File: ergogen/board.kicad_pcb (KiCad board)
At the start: 2 copper layers, 154.2 x 107.9 mm, 58 parts

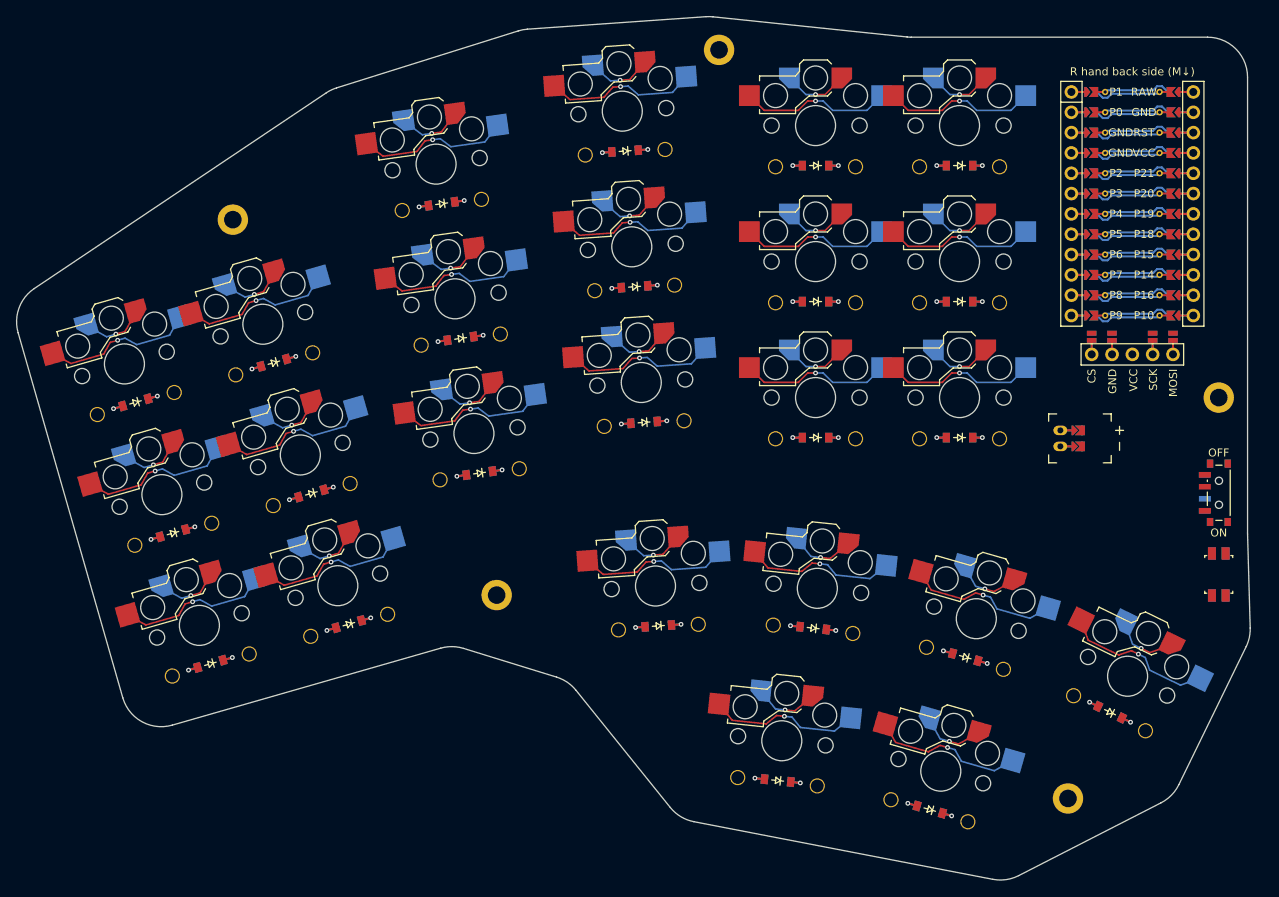
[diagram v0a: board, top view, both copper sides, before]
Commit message: making layout changes for easier routing
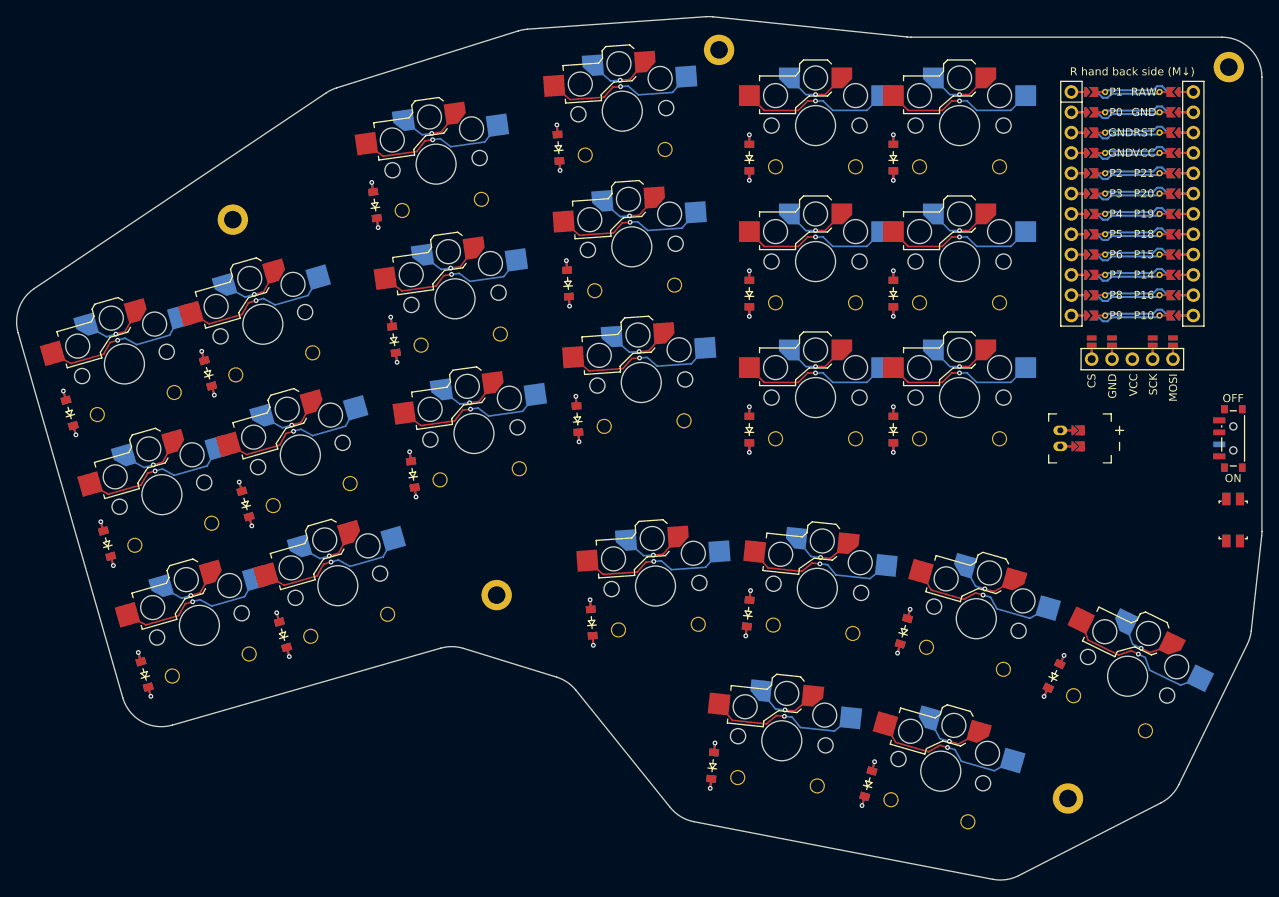
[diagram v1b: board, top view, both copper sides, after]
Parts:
- moved H5 41.3 mm to (278.7, 80.2)
- moved D7 8.34 mm to (176.7, 131.1), turned to 98 degrees
- moved D8 8.34 mm to (174.3, 114.3), turned to 98 degrees
- moved D9 8.34 mm to (171.9, 97.5), turned to 98 degrees
- moved D22 8.34 mm to (256.8, 156.3), turned to 64 degrees
- moved D21 8.34 mm to (238.1, 150.7), turned to 74 degrees
- moved D24 8.34 mm to (233.6, 169.8), turned to 74 degrees
- moved D19 8.34 mm to (199.0, 149.6), turned to 94 degrees
- moved D10 8.34 mm to (197.3, 124.2), turned to 94 degrees
- moved D11 8.34 mm to (196.1, 107.2), turned to 94 degrees
- moved D12 8.34 mm to (194.9, 90.3), turned to 94 degrees
- moved D1 8.34 mm to (143.1, 156.1), turned to 106 degrees
- moved D2 8.34 mm to (138.5, 139.8), turned to 106 degrees
- moved D3 8.34 mm to (133.8, 123.4), turned to 106 degrees
- moved D4 8.34 mm to (160.5, 151.2), turned to 106 degrees
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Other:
- board size 154.2 x 107.9 mm -> 155.7 x 107.9 mm
